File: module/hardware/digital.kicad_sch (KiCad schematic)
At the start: 34 parts, among them J10 Conn_01x03, J11 Conn_01x03, J12 Conn_01x03, J5 Conn_01x03_Male, J6 Conn_01x03_Male, J7 Conn_01x03, J8 Conn_01x03, J9 Conn_01x05_Male, SW2 SW_Push, U8 W25Q128JVS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

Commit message: Begin digital side routing
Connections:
- net GPIO4_BTN0: now also U9.35 (GPIO23); no longer U9.6 (GPIO4)
- net GPIO5_BTN1: now also U9.36 (GPIO24); no longer U9.7 (GPIO5)
- net _USB_D-: now reaches R17.2, U9.46 (USB_DM)
- net _USB_D+: now reaches R16.2, U9.47 (USB_DP)
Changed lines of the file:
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@@
   (junction (at 90.17 130.81) (diameter 0) (color 0 0 0 0)
   )
-  (no_connect (at 293.37 128.27))
+  (no_connect (at 293.37 77.47))
+  (no_connect (at 293.37 80.01))
   (no_connect (at 293.37 130.81))
   (no_connect (at 293.37 105.41))
   (no_connect (at 293.37 120.65))
   (no_connect (at 293.37 123.19))
-  (no_connect (at 293.37 125.73))
   (no_connect (at 293.37 100.33))
   (no_connect (at 293.37 97.79))
@@
     (stroke (width 0) (type default) (color 0 0 0 0))
   )
-  (wire (pts (xy 308.61 80.01) (xy 293.37 80.01))
+  (wire (pts (xy 308.61 128.27) (xy 293.37 128.27))
     (stroke (width 0) (type default) (color 0 0 0 0))
   )
@@
     (stroke (width 0) (type default) (color 0 0 0 0))
   )
-  (wire (pts (xy 308.61 77.47) (xy 293.37 77.47))
+  (wire (pts (xy 308.61 125.73) (xy 293.37 125.73))
     (stroke (width 0) (type default) (color 0 0 0 0))
   )
@@
     (effects (font (size 1.27 1.27)) (justify right bottom))
   )
+  (label "_USB_D-" (at 233.68 77.47 0)
+    (effects (font (size 1.27 1.27)) (justify left bottom))
+  )
   (label "GPIO28_ADC2" (at 111.76 149.86 0)
     (effects (font (size 1.27 1.27)) (justify left bottom))
   )
-  (label "GPIO4_BTN0" (at 308.61 77.47 180)
+  (label "GPIO4_BTN0" (at 308.61 125.73 180)
     (effects (font (size 1.27 1.27)) (justify right bottom))
   )
@@
     (effects (font (size 1.27 1.27)) (justify right bottom))
   )
+  (label "_USB_D+" (at 233.68 74.93 0)
+    (effects (font (size 1.27 1.27)) (justify left bottom))
+  )
   (label "GPIO28_ADC2" (at 308.61 140.97 180)
     (effects (font (size 1.27 1.27)) (justify right bottom))
@@
     (effects (font (size 1.27 1.27)) (justify left bottom))
   )
-  (label "GPIO5_BTN1" (at 308.61 80.01 180)
-    (effects (font (size 1.27 1.27)) (justify right bottom))
-  )
+  (label "GPIO5_BTN1" (at 308.61 128.27 180)
+    (effects (font (size 1.27 1.27)) (justify right bottom))
+  )

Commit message: Ground plane
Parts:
- added R19, R20: 10k, Resistor_SMD:R_0603_1608Metric_Pad0.98x0.95mm_HandSolder, symbol Device:R
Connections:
- net +3V3: now also R19.2, R20.2
- net GPIO4_BTN0: now also R19.1
- net GPIO5_BTN1: now also R20.1
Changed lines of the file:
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@@
   (junction (at 318.77 54.61) (diameter 0) (color 0 0 0 0)
   )
+  (junction (at 69.85 59.69) (diameter 0) (color 0 0 0 0)
+  )
   (junction (at 92.71 213.36) (diameter 0) (color 0 0 0 0)
   )
@@
   (junction (at 295.91 40.64) (diameter 0) (color 0 0 0 0)
   )
+  (junction (at 62.23 62.23) (diameter 0) (color 0 0 0 0)
+  )
   (junction (at 341.63 54.61) (diameter 0) (color 0 0 0 0)
   )
@@
   (junction (at 128.27 185.42) (diameter 0) (color 0 0 0 0)
   )
+  (junction (at 69.85 83.82) (diameter 0) (color 0 0 0 0)
+  )
   (junction (at 254 40.64) (diameter 0) (color 0 0 0 0)
   )
@@
   )
   (junction (at 78.74 144.78) (diameter 0) (color 0 0 0 0)
+  )
+  (junction (at 62.23 86.36) (diameter 0) (color 0 0 0 0)
   )
   (junction (at 231.14 40.64) (diameter 0) (color 0 0 0 0)
@@
     (stroke (width 0) (type default) (color 0 0 0 0))
   )
+  (wire (pts (xy 62.23 59.69) (xy 62.23 62.23))
+    (stroke (width 0) (type default) (color 0 0 0 0))
+  )
   (wire (pts (xy 214.63 123.19) (xy 229.87 123.19))
     (stroke (width 0) (type default) (color 0 0 0 0))
@@
     (stroke (width 0) (type default) (color 0 0 0 0))
   )
+  (wire (pts (xy 62.23 86.36) (xy 72.39 86.36))
+    (stroke (width 0) (type default) (color 0 0 0 0))
+  )
   (wire (pts (xy 231.14 36.83) (xy 231.14 40.64))
     (stroke (width 0) (type default) (color 0 0 0 0))
@@
     (stroke (width 0) (type default) (color 0 0 0 0))
   )
+  (wire (pts (xy 62.23 83.82) (xy 62.23 86.36))
+    (stroke (width 0) (type default) (color 0 0 0 0))
+  )
   (wire (pts (xy 295.91 52.07) (xy 295.91 54.61))
     (stroke (width 0) (type default) (color 0 0 0 0))
@@
     (stroke (width 0) (type default) (color 0 0 0 0))
   )
+  (wire (pts (xy 62.23 62.23) (xy 72.39 62.23))
+    (stroke (width 0) (type default) (color 0 0 0 0))
+  )
   (wire (pts (xy 69.85 64.77) (xy 72.39 64.77))
     (stroke (width 0) (type default) (color 0 0 0 0))
@@
     (stroke (width 0) (type default) (color 0 0 0 0))
   )
-  (wire (pts (xy 57.15 62.23) (xy 72.39 62.23))
+  (wire (pts (xy 48.26 62.23) (xy 62.23 62.23))
     (stroke (width 0) (type default) (color 0 0 0 0))
   )
@@
     (stroke (width 0) (type default) (color 0 0 0 0))
   )
-  (wire (pts (xy 57.15 86.36) (xy 72.39 86.36))
+  (wire (pts (xy 48.26 86.36) (xy 62.23 86.36))
     (stroke (width 0) (type default) (color 0 0 0 0))
   )
@@
     (effects (font (size 1.27 1.27)) (justify right bottom))
   )
-  (label "GPIO4_BTN0" (at 57.15 62.23 0)
+  (label "GPIO4_BTN0" (at 48.26 62.23 0)
     (effects (font (size 1.27 1.27)) (justify left bottom))
   )
@@
     (effects (font (size 1.27 1.27)) (justify left bottom))
   )
-  (label "GPIO5_BTN1" (at 57.15 86.36 0)
+  (label "GPIO5_BTN1" (at 48.26 86.36 0)
     (effects (font (size 1.27 1.27)) (justify left bottom))
   )
@@
     (pin "1")
   )
+  (symbol (lib_id "Device:R") (at 66.04 59.69 90) (unit 1)
+    (in_bom yes) (on_board yes)
+    (property "Reference" "R19" (id 0) (at 66.04 57.15 90))
+    (property "Value" "10k" (id 1) (at 66.04 59.69 90))
+    (property "Footprint" "Resistor_SMD:R_0603_1608Metric_Pad0.98x0.95mm_HandSolder" (id 2) (at 66.04 61.468 90)
+      (effects (font (size 1.27 1.27)) hide)
+    )
+    (property "Datasheet" "~" (id 3) (at 66.04 59.69 0)
+      (effects (font (size 1.27 1.27)) hide)
+    )
+    (pin "1")
+    (pin "2")
+  )
   (symbol (lib_id "Connector:Conn_01x03_Male") (at 77.47 86.36 180) (unit 1)
     (in_bom yes) (on_board yes) (fields_autoplaced)
@@
       (effects (font (size 1.27 1.27)) hide)
     )
+    (pin "1")
+    (pin "2")
+  )
+  (symbol (lib_id "Device:R") (at 66.04 83.82 90) (unit 1)
+    (in_bom yes) (on_board yes)
+    (property "Reference" "R20" (id 0) (at 66.04 81.28 90))
+    (property "Value" "10k" (id 1) (at 66.04 83.82 90))
+    (property "Footprint" "Resistor_SMD:R_0603_1608Metric_Pad0.98x0.95mm_HandSolder" (id 2) (at 66.04 85.598 90)
+      (effects (font (size 1.27 1.27)) hide)
+    )
+    (property "Datasheet" "~" (id 3) (at 66.04 83.82 0)
+      (effects (font (size 1.27 1.27)) hide)
+    )

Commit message: Route/move USB
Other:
- moved on the sheet: R19, R20
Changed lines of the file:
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@@
   (junction (at 318.77 40.64) (diameter 0) (color 0 0 0 0)
   )
+  (junction (at 58.42 86.36) (diameter 0) (color 0 0 0 0)
+  )
   (junction (at 240.03 143.51) (diameter 0) (color 0 0 0 0)
   )
@@
   (junction (at 92.71 213.36) (diameter 0) (color 0 0 0 0)
   )
+  (junction (at 58.42 62.23) (diameter 0) (color 0 0 0 0)
+  )
   (junction (at 242.57 55.88) (diameter 0) (color 0 0 0 0)
   )
@@
   (junction (at 295.91 40.64) (diameter 0) (color 0 0 0 0)
   )
-  (junction (at 62.23 62.23) (diameter 0) (color 0 0 0 0)
-  )
   (junction (at 341.63 54.61) (diameter 0) (color 0 0 0 0)
   )
@@
   )
   (junction (at 78.74 144.78) (diameter 0) (color 0 0 0 0)
-  )
-  (junction (at 62.23 86.36) (diameter 0) (color 0 0 0 0)
   )
   (junction (at 231.14 40.64) (diameter 0) (color 0 0 0 0)
@@
     (stroke (width 0) (type default) (color 0 0 0 0))
   )
-  (wire (pts (xy 62.23 59.69) (xy 62.23 62.23))
+  (wire (pts (xy 58.42 59.69) (xy 58.42 62.23))
     (stroke (width 0) (type default) (color 0 0 0 0))
   )
@@
     (stroke (width 0) (type default) (color 0 0 0 0))
   )
+  (wire (pts (xy 58.42 59.69) (xy 59.69 59.69))
+    (stroke (width 0) (type default) (color 0 0 0 0))
+  )
   (wire (pts (xy 114.3 128.27) (xy 127 128.27))
     (stroke (width 0) (type default) (color 0 0 0 0))
   )
+  (wire (pts (xy 58.42 86.36) (xy 72.39 86.36))
+    (stroke (width 0) (type default) (color 0 0 0 0))
+  )
   (wire (pts (xy 114.3 120.65) (xy 114.3 123.19))
     (stroke (width 0) (type default) (color 0 0 0 0))
@@
     (stroke (width 0) (type default) (color 0 0 0 0))
   )
-  (wire (pts (xy 62.23 86.36) (xy 72.39 86.36))
-    (stroke (width 0) (type default) (color 0 0 0 0))
-  )
   (wire (pts (xy 231.14 36.83) (xy 231.14 40.64))
     (stroke (width 0) (type default) (color 0 0 0 0))
@@
     (stroke (width 0) (type default) (color 0 0 0 0))
   )
-  (wire (pts (xy 62.23 83.82) (xy 62.23 86.36))
+  (wire (pts (xy 58.42 83.82) (xy 58.42 86.36))
     (stroke (width 0) (type default) (color 0 0 0 0))
   )
@@
     (stroke (width 0) (type default) (color 0 0 0 0))
   )
-  (wire (pts (xy 62.23 62.23) (xy 72.39 62.23))
+  (wire (pts (xy 58.42 62.23) (xy 72.39 62.23))
     (stroke (width 0) (type default) (color 0 0 0 0))
   )
@@
     (stroke (width 0) (type default) (color 0 0 0 0))
   )
-  (wire (pts (xy 48.26 62.23) (xy 62.23 62.23))
+  (wire (pts (xy 45.72 62.23) (xy 58.42 62.23))
     (stroke (width 0) (type default) (color 0 0 0 0))
   )
@@
     (stroke (width 0) (type default) (color 0 0 0 0))
   )
+  (wire (pts (xy 67.31 59.69) (xy 69.85 59.69))
+    (stroke (width 0) (type default) (color 0 0 0 0))
+  )
+  (wire (pts (xy 58.42 83.82) (xy 59.69 83.82))
+    (stroke (width 0) (type default) (color 0 0 0 0))
+  )
   (wire (pts (xy 240.03 143.51) (xy 240.03 153.67))
     (stroke (width 0) (type default) (color 0 0 0 0))
@@
     (stroke (width 0) (type default) (color 0 0 0 0))
   )
-  (wire (pts (xy 48.26 86.36) (xy 62.23 86.36))
+  (wire (pts (xy 45.72 86.36) (xy 58.42 86.36))
     (stroke (width 0) (type default) (color 0 0 0 0))
   )
@@
   )
   (wire (pts (xy 242.57 90.17) (xy 233.68 90.17))
+    (stroke (width 0) (type default) (color 0 0 0 0))
+  )
+  (wire (pts (xy 67.31 83.82) (xy 69.85 83.82))
     (stroke (width 0) (type default) (color 0 0 0 0))
   )
@@
     (effects (font (size 1.27 1.27)) (justify right bottom))
   )
-  (label "GPIO4_BTN0" (at 48.26 62.23 0)
+  (label "GPIO4_BTN0" (at 45.72 62.23 0)
     (effects (font (size 1.27 1.27)) (justify left bottom))
   )
@@
     (effects (font (size 1.27 1.27)) (justify left bottom))
   )
-  (label "GPIO5_BTN1" (at 48.26 86.36 0)
+  (label "GPIO5_BTN1" (at 45.72 86.36 0)
     (effects (font (size 1.27 1.27)) (justify left bottom))
   )
@@
     (pin "1")
   )
-  (symbol (lib_id "Device:R") (at 66.04 59.69 90) (unit 1)
+  (symbol (lib_id "Device:R") (at 63.5 59.69 90) (unit 1)
     (in_bom yes) (on_board yes)
-    (property "Reference" "R19" (id 0) (at 66.04 57.15 90))
-    (property "Value" "10k" (id 1) (at 66.04 59.69 90))
-    (property "Footprint" "Resistor_SMD:R_0603_1608Metric_Pad0.98x0.95mm_HandSolder" (id 2) (at 66.04 61.468 90)
-      (effects (font (size 1.27 1.27)) hide)
-    )
-    (property "Datasheet" "~" (id 3) (at 66.04 59.69 0)
+    (property "Reference" "R19" (id 0) (at 63.5 57.15 90))
+    (property "Value" "10k" (id 1) (at 63.5 59.69 90))
+    (property "Footprint" "Resistor_SMD:R_0603_1608Metric_Pad0.98x0.95mm_HandSolder" (id 2) (at 63.5 61.468 90)
+      (effects (font (size 1.27 1.27)) hide)
+    )
+    (property "Datasheet" "~" (id 3) (at 63.5 59.69 0)
       (effects (font (size 1.27 1.27)) hide)
     )
@@
     (pin "2")
   )
-  (symbol (lib_id "Device:R") (at 66.04 83.82 90) (unit 1)
+  (symbol (lib_id "Device:R") (at 63.5 83.82 90) (unit 1)
     (in_bom yes) (on_board yes)
-    (property "Reference" "R20" (id 0) (at 66.04 81.28 90))
-    (property "Value" "10k" (id 1) (at 66.04 83.82 90))
-    (property "Footprint" "Resistor_SMD:R_0603_1608Metric_Pad0.98x0.95mm_HandSolder" (id 2) (at 66.04 85.598 90)
-      (effects (font (size 1.27 1.27)) hide)
-    )
-    (property "Datasheet" "~" (id 3) (at 66.04 83.82 0)
-      (effects (font (size 1.27 1.27)) hide)
-    )
+    (property "Reference" "R20" (id 0) (at 63.5 81.28 90))
+    (property "Value" "10k" (id 1) (at 63.5 83.82 90))
+    (property "Footprint" "Resistor_SMD:R_0603_1608Metric_Pad0.98x0.95mm_HandSolder" (id 2) (at 63.5 85.598 90)
+      (effects (font (size 1.27 1.27)) hide)
+    )
+    (property "Datasheet" "~" (id 3) (at 63.5 83.82 0)
+      (effects (font (size 1.27 1.27)) hide)
+    )

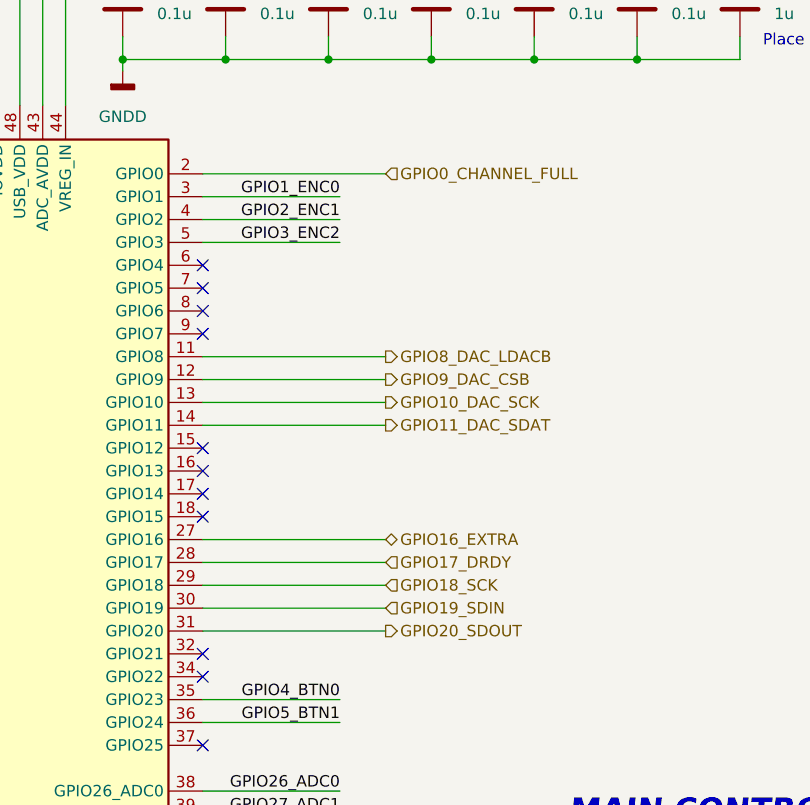
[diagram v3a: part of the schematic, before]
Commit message: Reorder RP2040 GPIO lines for improved routability
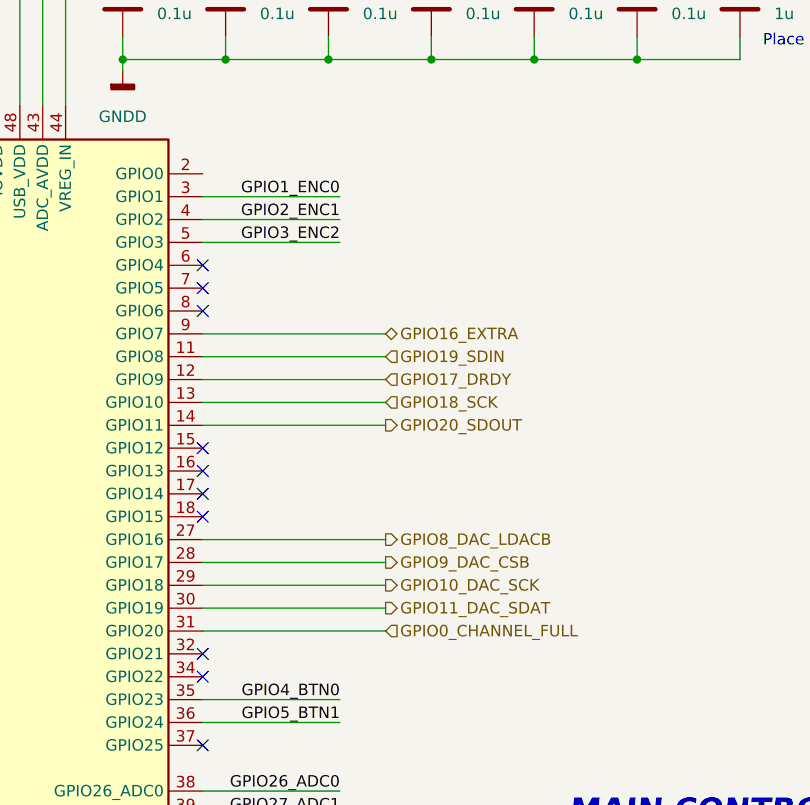
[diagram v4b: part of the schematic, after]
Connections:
- net GPIO0_CHANNEL_FULL: now also U9.31 (GPIO20); no longer U9.2 (GPIO0)
- net GPIO10_DAC_SCK: now also U9.29 (GPIO18); no longer U9.13 (GPIO10)
- net GPIO11_DAC_SDAT: now also U9.30 (GPIO19); no longer U9.14 (GPIO11)
- net GPIO16_EXTRA: now also U9.9 (GPIO7); no longer U9.27 (GPIO16)
- net GPIO17_DRDY: now also U9.12 (GPIO9); no longer U9.28 (GPIO17)
- net GPIO18_SCK: now also U9.13 (GPIO10); no longer U9.29 (GPIO18)
- net GPIO19_SDIN: now also U9.11 (GPIO8); no longer U9.30 (GPIO19)
- net GPIO20_SDOUT: now also U9.14 (GPIO11); no longer U9.31 (GPIO20)
- net GPIO8_DAC_LDACB: now also U9.27 (GPIO16); no longer U9.11 (GPIO8)
- net GPIO9_DAC_CSB: now also U9.28 (GPIO17); no longer U9.12 (GPIO9)
- no-connect marks 11 -> 10

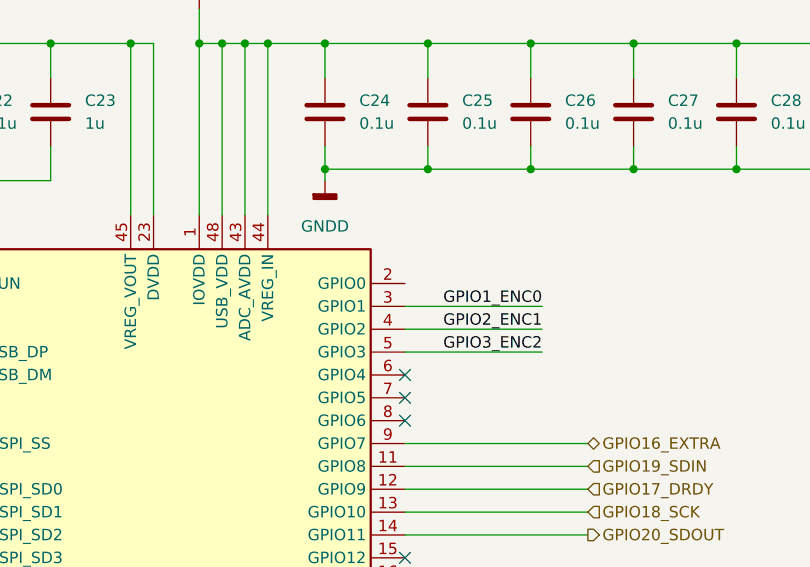
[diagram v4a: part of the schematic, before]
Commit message: Module Analog preliminaty routing complete
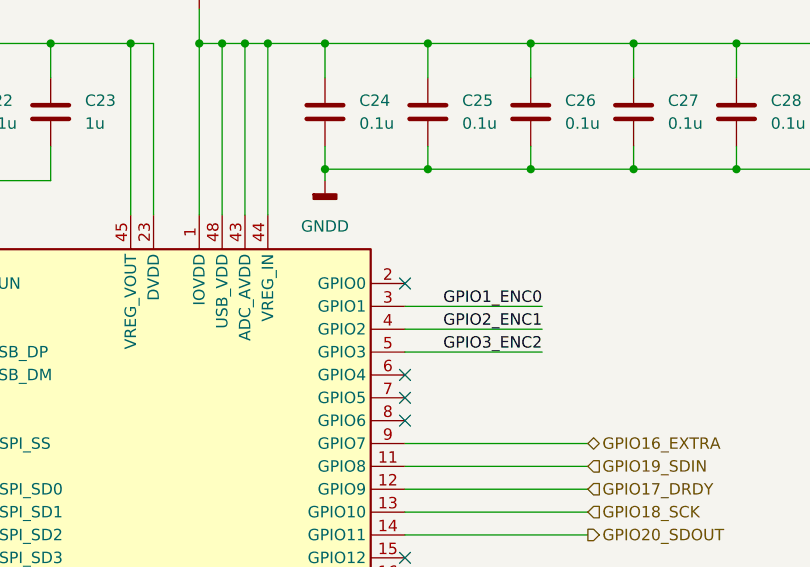
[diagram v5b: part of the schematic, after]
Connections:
- no-connect marks 10 -> 11
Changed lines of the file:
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@@
   (junction (at 90.17 130.81) (diameter 0) (color 0 0 0 0)
   )
+  (no_connect (at 293.37 67.31))
   (no_connect (at 293.37 77.47))
   (no_connect (at 293.37 80.01))
